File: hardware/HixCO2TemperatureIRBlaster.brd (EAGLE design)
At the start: 88.9 x 45.7 mm, 38 parts, among them J1 FTDI, J2 IEC320C8, J3 XH4P, Q1 AO3400, Q2 AO3400, U1 TSOP2238, U2 LM3940, U3 HLK-PM01, U4 DS18B20

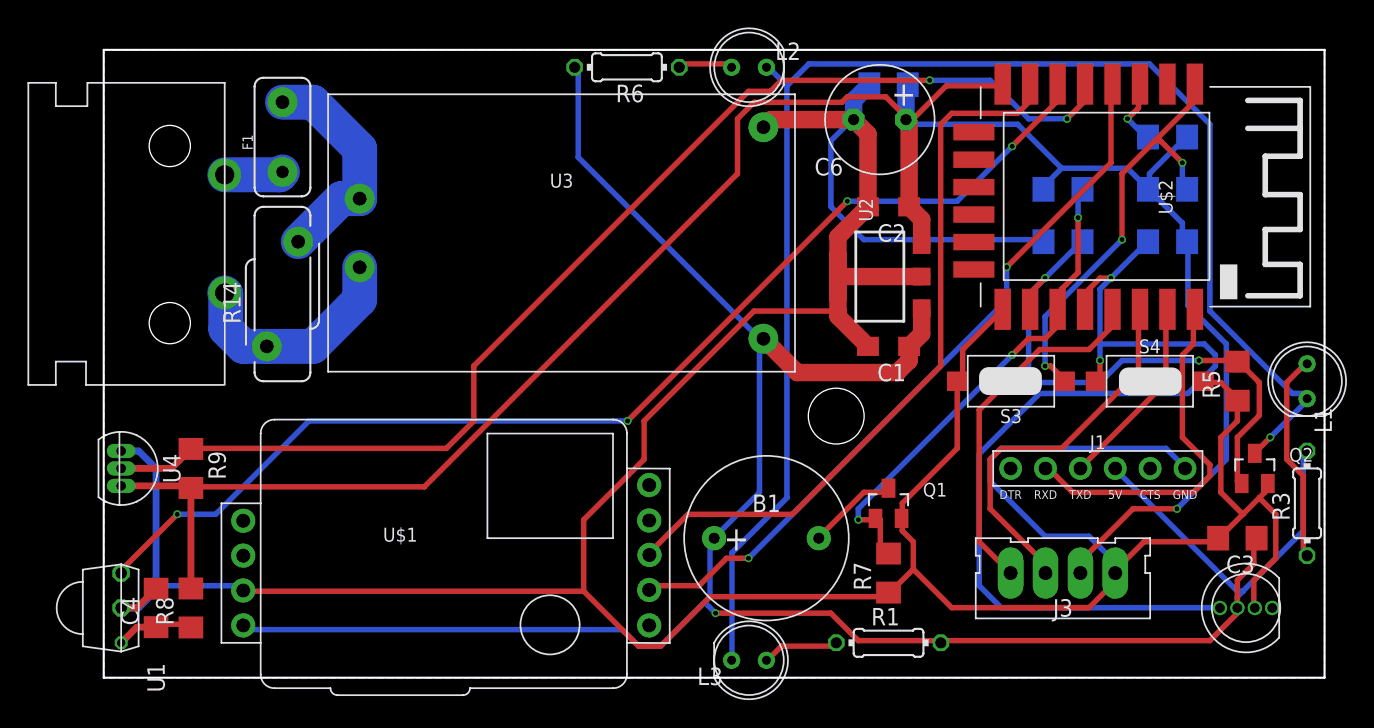
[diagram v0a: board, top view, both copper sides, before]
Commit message: Fixed short-circuit between 3.3V and 5.0V on board layout
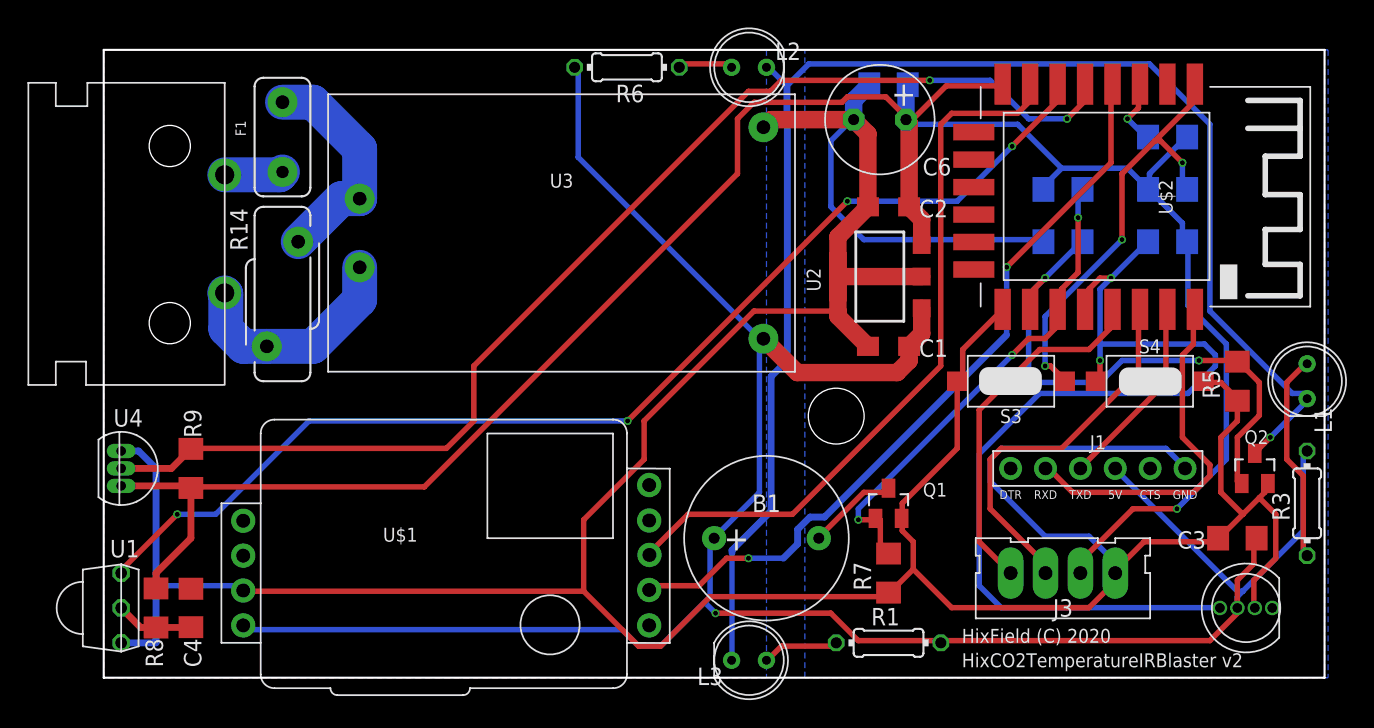
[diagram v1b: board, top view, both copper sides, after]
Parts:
- moved C4 2.54 mm to (-127.0, -261.6)
- moved R8 2.54 mm to (-129.5, -261.6)
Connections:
- net GND: now also U1.GND; no longer U1.VCC
- net N$6: now also U1.VCC; no longer U1.GND
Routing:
- net CO2_TX: track 53.8 -> 55.9 mm
- net 3.3V: track 163.2 -> 164.2 mm
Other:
- board text added: "HixCO2TemperatureIRBlaster v2"
- board text added: "HixField (C) 2020"
